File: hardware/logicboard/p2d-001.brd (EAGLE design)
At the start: 100 x 75 mm, 69 parts, among them IC1 74LS06N, IC2 4066N, IC3 MAX3468CPA, J1 MKR, J10 THS, J11 XLR, J2 GPIO, J3 Vcc, J4 RLY, J5 SPI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

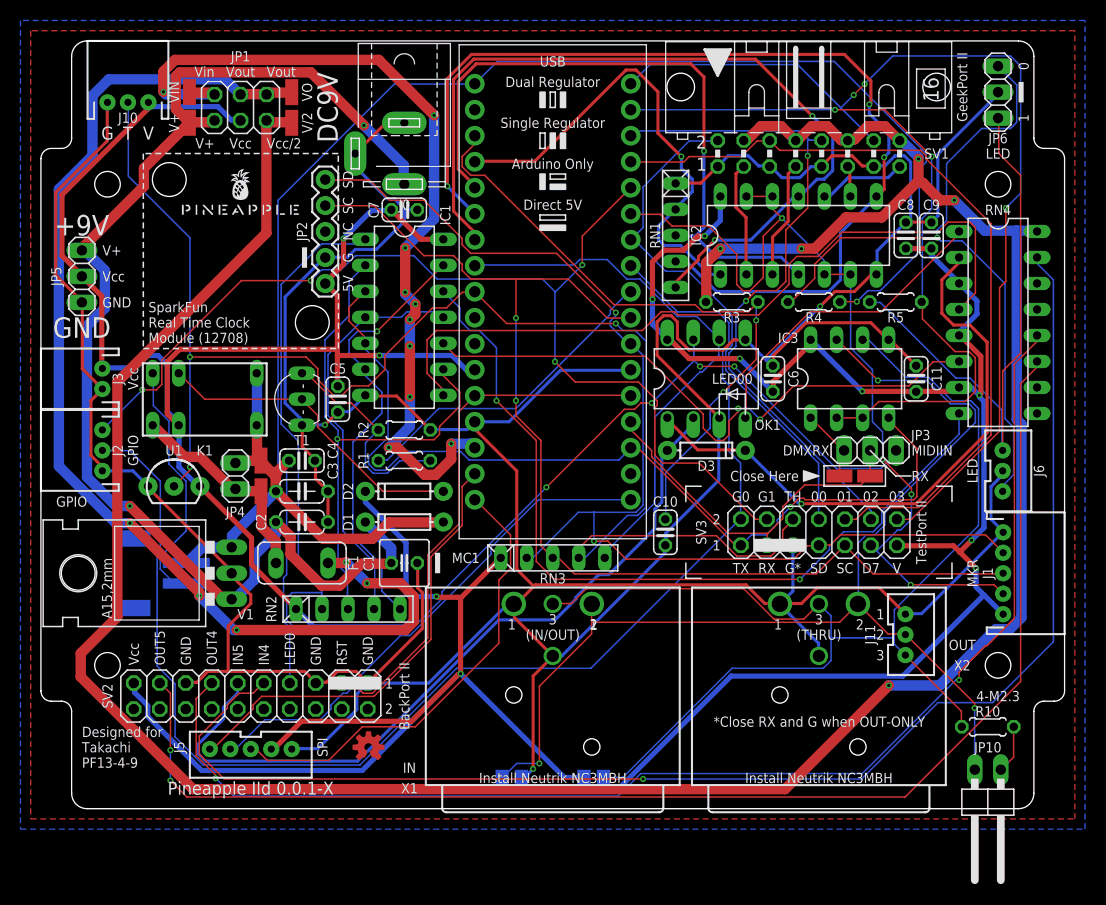
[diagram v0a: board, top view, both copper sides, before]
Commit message: Changed size of logic board to fit in the case.
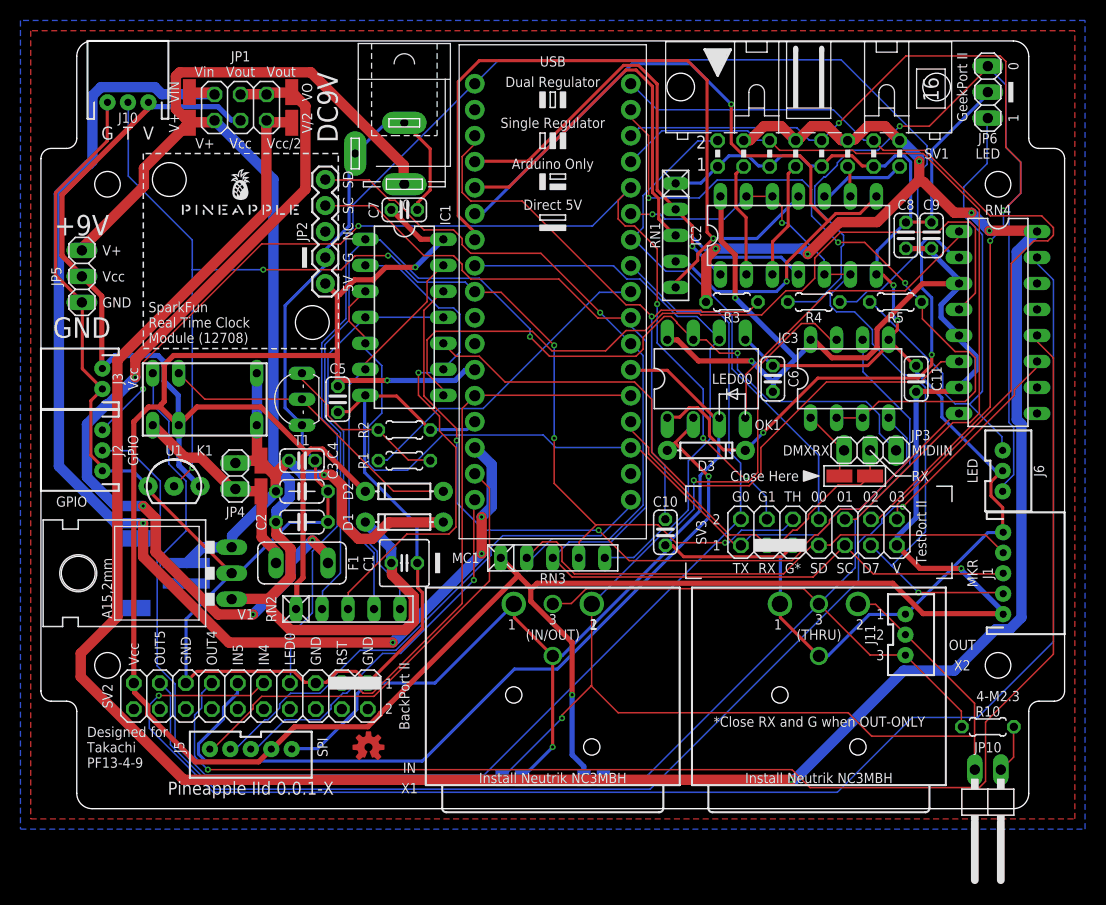
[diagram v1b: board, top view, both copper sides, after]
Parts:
- moved JP6 1.00 mm to (92.5, 70.0)
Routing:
- net VIN: track 85.7 -> 118.1 mm, vias 10 -> 4
- net GND: track 483.8 -> 451.9 mm
- net DTCT2: track 66.5 -> 92.9 mm, vias 2 -> 3
- net VOUT: track 112.5 -> 88.4 mm, vias 5 -> 4
- net MIN: track 128.0 -> 106.0 mm, vias 4 -> 2
- net ANLG2: track 97.8 -> 77.1 mm, vias 3 -> 2
- net THS: track 144.8 -> 124.5 mm, vias 3 -> 6
- net MORTN: track 130.3 -> 113.3 mm, vias 2 -> 1
- net DTCT3: track 97.8 -> 82.8 mm, vias 3 -> 0
- net DATA-: track 111.2 -> 125.8 mm, vias 3 -> 2
- net ANLG1: track 65.8 -> 52.0 mm, vias 1 -> 0
- net LED0A: track 69.9 -> 82.5 mm
- net DATA+: track 119.0 -> 106.6 mm
- net MISND: track 138.6 -> 149.6 mm
- net V+: track 126.0 -> 135.9 mm, vias 2 -> 0
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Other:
- outline, holes or cut-outs redrawn

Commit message: Change size of the logic board.
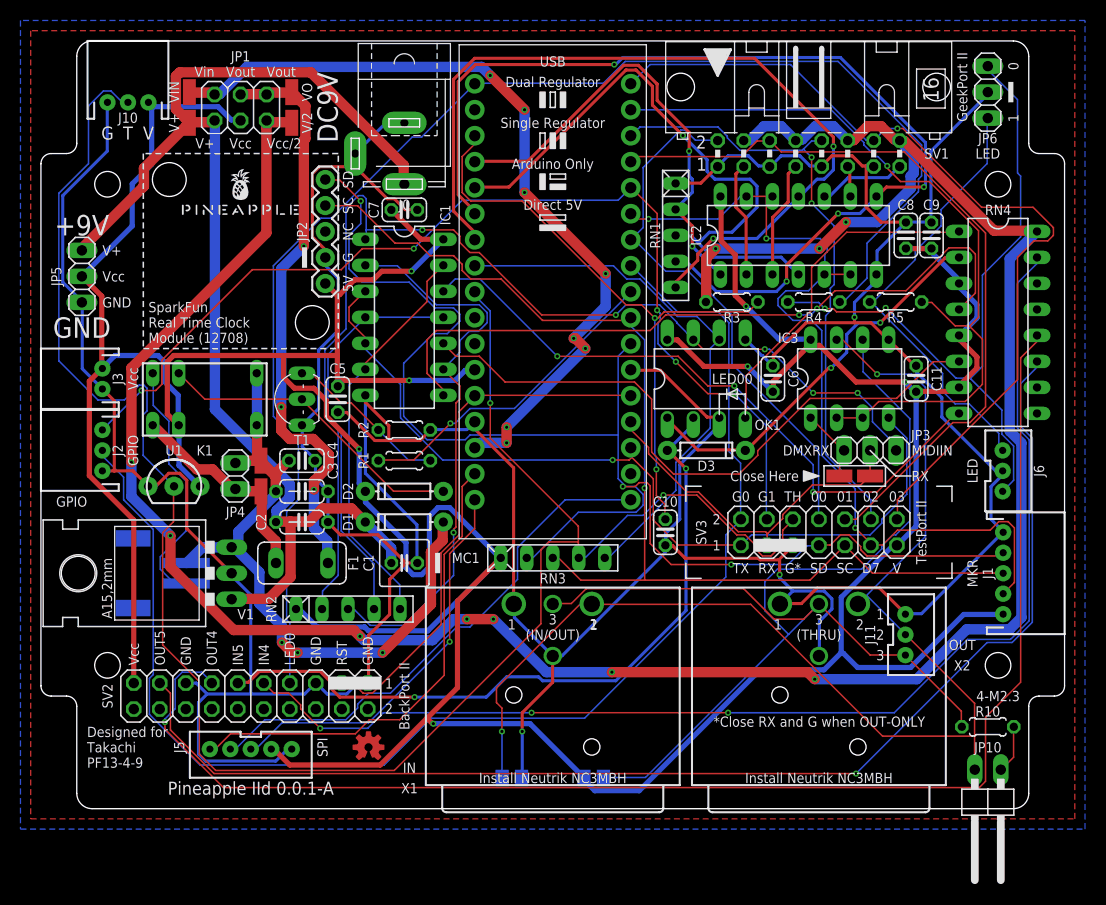
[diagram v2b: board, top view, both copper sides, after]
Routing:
- net THS: track 124.5 -> 190.9 mm, vias 6 -> 2
- net VIN: track 118.1 -> 79.9 mm, vias 4 -> 8
- net DTCT2: track 92.9 -> 60.0 mm, vias 3 -> 2
- net MISND: track 149.6 -> 117.9 mm, vias 1 -> 3
- net VOUT: track 88.4 -> 57.1 mm, vias 4 -> 3
- net ANLG2: track 77.1 -> 98.7 mm, vias 2 -> 4
- net VCC/2: track 271.5 -> 252.7 mm, vias 6 -> 10
- net SDA: track 118.3 -> 137.1 mm, vias 1 -> 3
- net GND: track 451.9 -> 470.1 mm
- net N$4: track 80.6 -> 64.3 mm, vias 2 -> 3
- net VOUTRAW: track 50.3 -> 66.4 mm, vias 1 -> 3
- net LED0A: track 82.5 -> 68.3 mm, vias 1 -> 2
- net V+: track 135.9 -> 122.3 mm
- net DATA+: track 106.6 -> 118.9 mm
- net MIRTN: track 81.4 -> 70.2 mm, vias 1 -> 2
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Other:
- outline, holes or cut-outs redrawn
- board text added: "Pineapple IId 0.0.1-A"
- board text removed: "Pineapple IId 0.0.1-X"

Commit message: Changed silk of JP10.
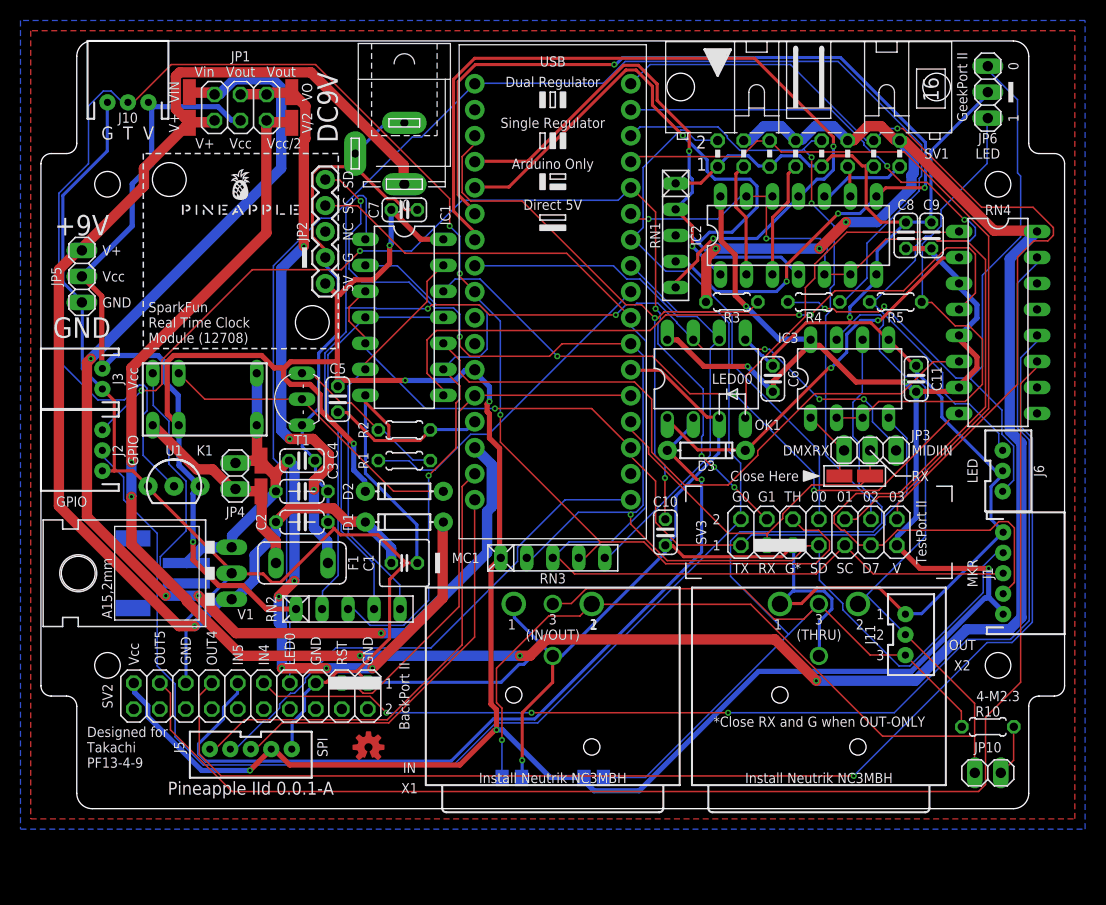
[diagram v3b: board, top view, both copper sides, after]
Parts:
- JP10: device pinhead:1X02/90 -> pinhead:1X02
- moved JP10 3.50 mm to (92.5, 3.50)
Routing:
- net VIN: track 79.9 -> 118.0 mm, vias 8 -> 4
- net VCC: track 436.3 -> 407.8 mm, vias 7 -> 11
- net THS: track 190.9 -> 162.9 mm, vias 2 -> 3
- net D7GATE: track 88.0 -> 107.8 mm, vias 3 -> 2
- net GND: track 470.1 -> 456.3 mm, vias 3 -> 2
- net MOSND: track 138.1 -> 125.1 mm
- net MIRTN: track 70.2 -> 82.3 mm, vias 2 -> 1
- net VOUTRAW: track 66.4 -> 76.5 mm, vias 3 -> 5
- net SDA: track 137.1 -> 127.6 mm
- net MORTN: track 123.7 -> 130.8 mm, vias 1 -> 0
- net DATA-: track 121.6 -> 127.5 mm, vias 2 -> 1
- net DATA+: track 118.9 -> 122.8 mm
- net V+: track 122.3 -> 125.8 mm, vias 0 -> 1
- net SCL: track 108.6 -> 111.7 mm, vias 1 -> 0
- net GPIO0: track 131.8 -> 128.9 mm
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
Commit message: Changed dimension of the logic board to fit the base panel.
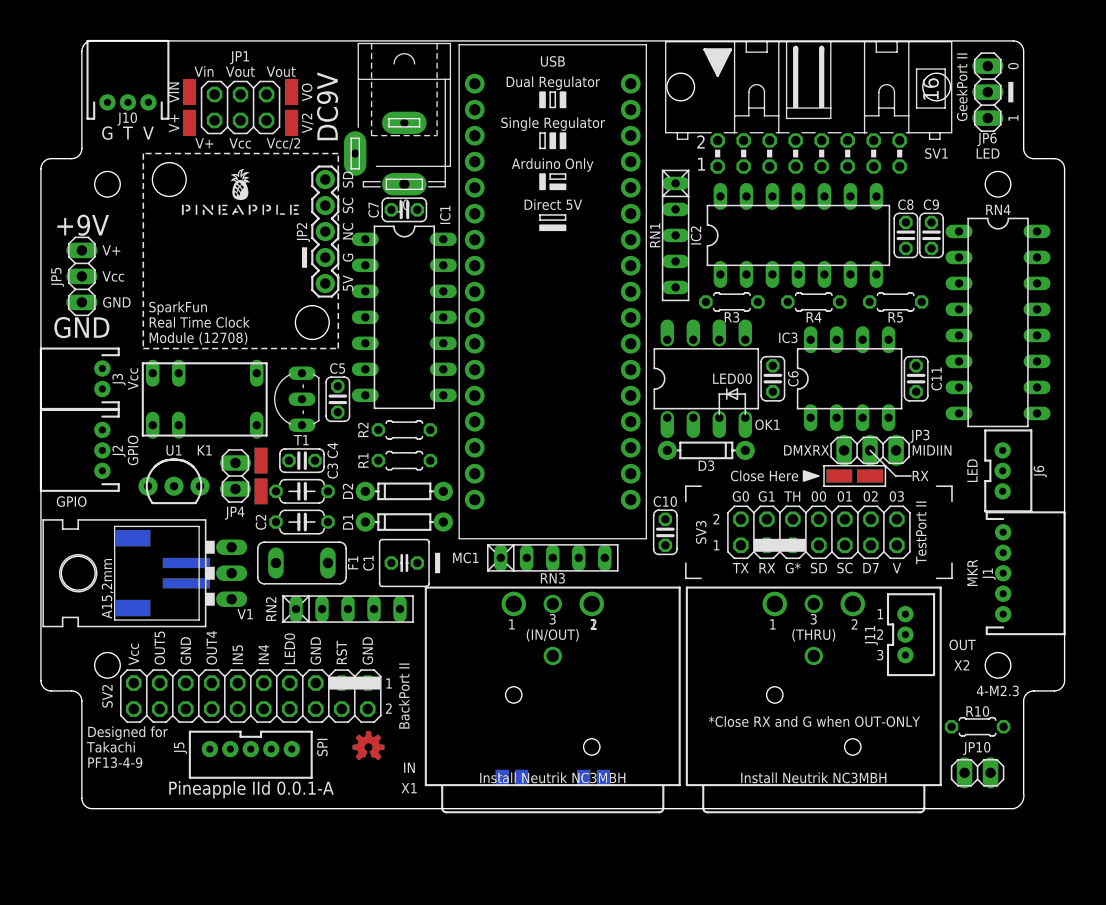
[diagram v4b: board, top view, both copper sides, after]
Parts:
- moved JP10 1.00 mm to (91.5, 3.50)
- moved R10 1.00 mm to (91.5, 8.00)
- moved X2 0.50 mm to (75.5, 20.0)
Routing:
- net GND: track 456.3 -> 0.00 mm, vias 2 -> 0
- net VCC: track 407.8 -> 0.00 mm, vias 11 -> 0
- net VCC/2: track 253.5 -> 0.00 mm, vias 8 -> 0
- net THS: track 162.9 -> 0.00 mm, vias 3 -> 0
- net LED0: track 135.2 -> 0.00 mm
- net MORTN: track 130.8 -> 0.00 mm
- net GPIO0: track 128.9 -> 0.00 mm
- net SDA: track 127.6 -> 0.00 mm, vias 3 -> 0
- net DATA-: track 127.5 -> 0.00 mm, vias 1 -> 0
- net V+: track 125.8 -> 0.00 mm, vias 1 -> 0
- net MOSND: track 125.1 -> 0.00 mm, vias 1 -> 0
- net DATA+: track 122.8 -> 0.00 mm
- net VIN: track 118.0 -> 0.00 mm, vias 4 -> 0
- net MISND: track 116.4 -> 0.00 mm, vias 3 -> 0
- net SCL: track 111.7 -> 0.00 mm
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- removed copper zone on layer 1, net GND
- removed copper zone on layer 16, net GND
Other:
- outline, holes or cut-outs redrawn
